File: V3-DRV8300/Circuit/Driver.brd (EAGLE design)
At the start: 61 x 56 mm, 37 parts, among them IC1 DRV8303DCA

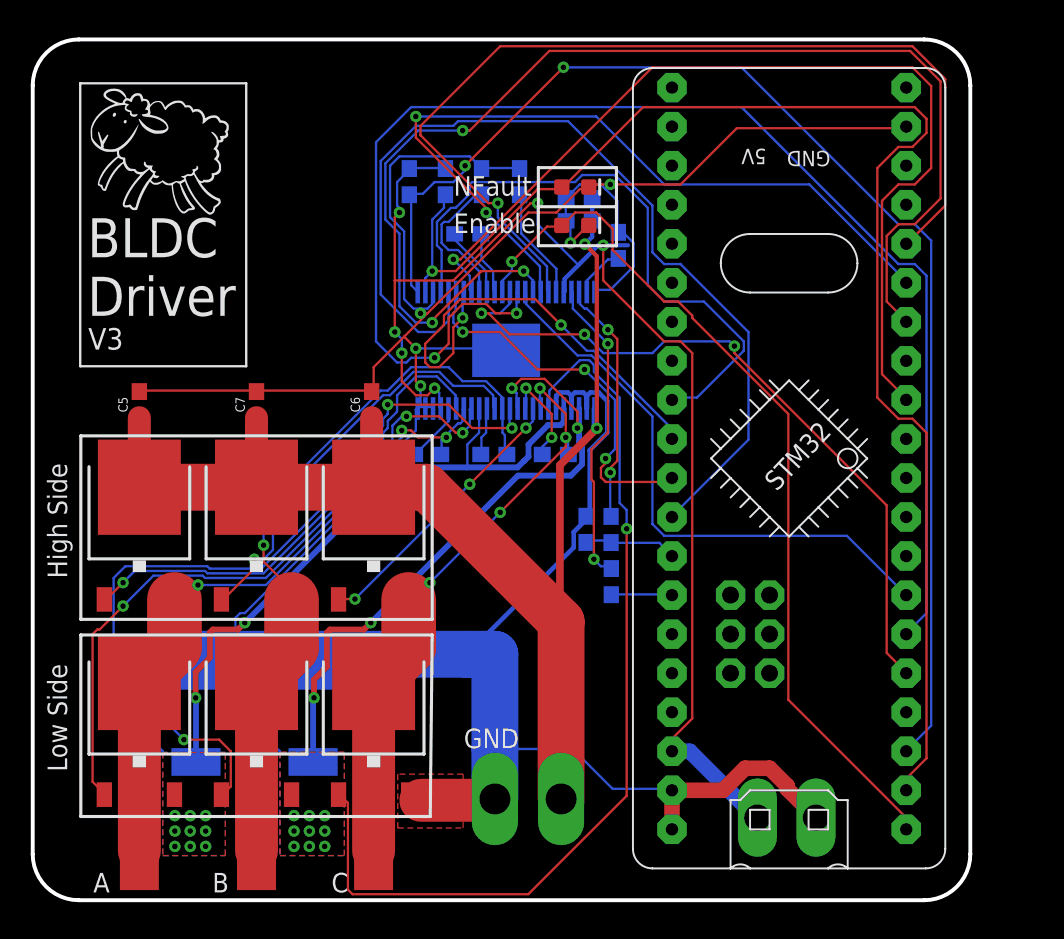
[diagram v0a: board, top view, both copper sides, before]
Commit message: Prepared for V3-DRV8300 PCB routing
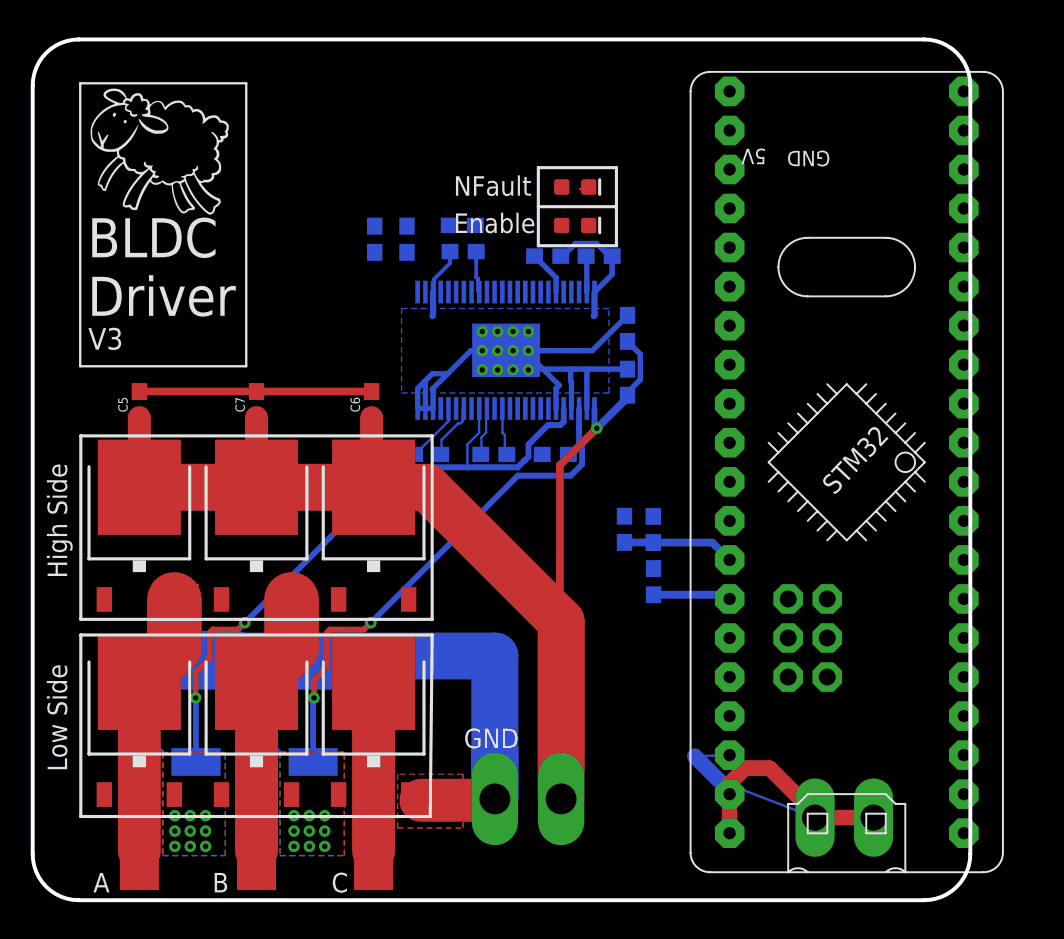
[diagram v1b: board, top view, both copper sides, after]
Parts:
- removed C10, C11: 1.0uF, SparkFun-Capacitors:0603
- added AVDD_CAP, DVDD_CAP: 1.0uF, SparkFun-Capacitors:0603
- moved C15 12.4 mm to (37.7, 32.7), turned to 90 degrees
- moved C14 7.68 mm to (37.7, 36.2), turned to 90 degrees
- moved C8 4.71 mm to (27.0, 41.2), turned to 0 degrees
- moved R6 4.51 mm to (23.4, 42.0)
- moved R4 4.37 mm to (21.2, 42.0)
- moved U$1 3.76 mm to (49.4, 33.8)
- moved 5V 3.75 mm to (51.8, 4.37)
- moved R5 2.75 mm to (39.4, 19.7)
- moved R7 2.75 mm to (39.4, 23.1)
- moved C16 2.50 mm to (37.5, 23.1)
- moved C9 0.65 mm to (26.9, 42.9), turned to 180 degrees
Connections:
- net GND: now also AVDD_CAP.2, DVDD_CAP.1; no longer C10.1, C11.2
- net N$43: now also DVDD_CAP.2; no longer C10.2
- net N$47: now also AVDD_CAP.1; no longer C11.1
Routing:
- net GND: track 232.6 -> 137.4 mm, vias 5 -> 12
- net PA9: track 92.1 -> 0.00 mm, vias 2 -> 0
- net PB13: track 91.8 -> 0.00 mm, vias 1 -> 0
- net PB14: track 82.7 -> 0.00 mm, vias 2 -> 0
- net PB6: track 79.5 -> 0.00 mm, vias 3 -> 0
- net VCC: track 87.3 -> 11.3 mm, vias 6 -> 0
- net PB8: track 63.6 -> 0.00 mm, vias 1 -> 0
- net PA7: track 62.8 -> 0.00 mm
- net PB4: track 62.4 -> 0.00 mm, vias 1 -> 0
- net GL_C: track 61.3 -> 0.00 mm, vias 1 -> 0
- net PB12: track 58.1 -> 0.00 mm, vias 1 -> 0
- net GL_B: track 54.3 -> 0.00 mm, vias 3 -> 0
- net PB7: track 51.2 -> 0.00 mm, vias 2 -> 0
- net PA8: track 46.7 -> 0.00 mm, vias 3 -> 0
- net GL_A: track 44.1 -> 0.00 mm, vias 3 -> 0
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- added copper zone on layer 16, net GND

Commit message: Prepared for V3-DRV8300 PCB routing 3
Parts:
- moved C9 1.75 mm to (26.9, 44.6)
- moved AVDD_CAP 1.25 mm to (35.9, 42.1)
- moved DVDD_CAP 1.25 mm to (32.5, 42.1)
- moved R4 1.25 mm to (21.2, 43.2)
- moved R6 1.25 mm to (23.4, 43.2)
- moved C14 1.00 mm to (38.7, 36.2)
- moved C15 1.00 mm to (38.7, 32.7)
- moved C8 1.00 mm to (27.0, 42.2)
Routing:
- net N$47: track 3.11 -> 4.36 mm
- net N$43: track 2.94 -> 4.19 mm
- net N$32: track 2.86 -> 3.86 mm
- net VIN: track 91.3 -> 92.2 mm
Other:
- board size 61 x 56 mm -> 65 x 56.8 mm

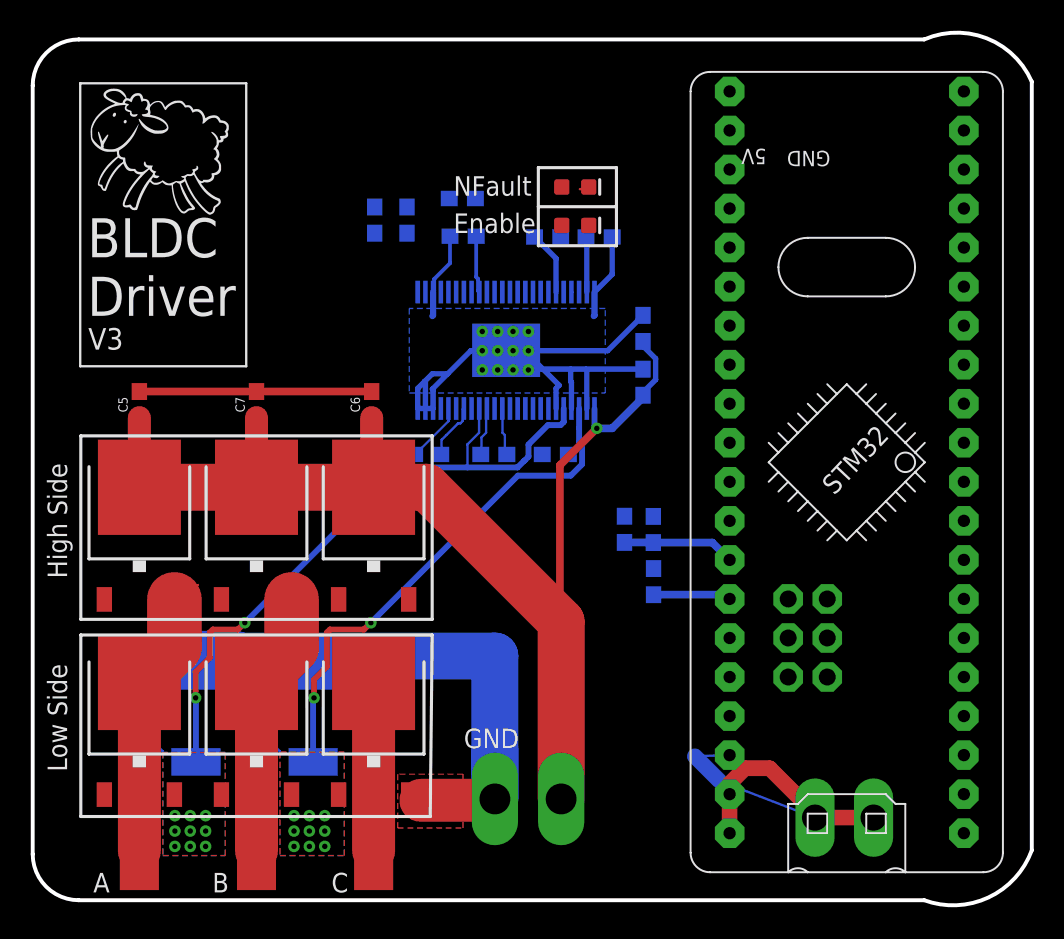
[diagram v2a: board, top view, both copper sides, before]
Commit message: V3-DRV8303 PCB Routed
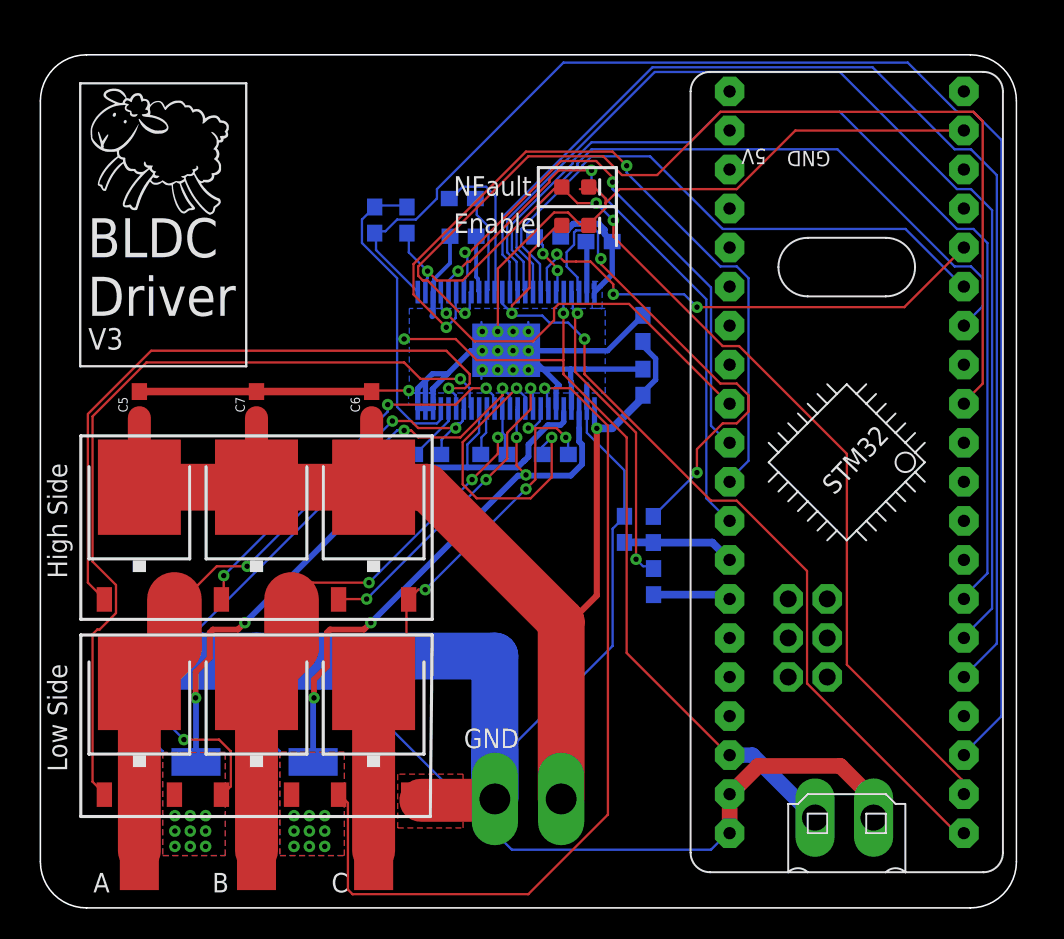
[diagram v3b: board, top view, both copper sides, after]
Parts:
- moved AVDD_CAP 0.30 mm to (35.9, 41.9)
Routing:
- net GND: track 137.6 -> 249.8 mm, vias 12 -> 13
- net PB14: track 0.00 -> 93.9 mm
- net PA8: track 0.00 -> 77.7 mm
- net PA9: track 0.00 -> 72.8 mm
- net PB13: track 0.00 -> 67.8 mm, vias 0 -> 3
- net PB4: track 0.00 -> 67.3 mm, vias 0 -> 1
- net PA10: track 0.00 -> 66.1 mm
- net VCC: track 11.3 -> 74.1 mm, vias 0 -> 2
- net PB12: track 0.00 -> 57.9 mm, vias 0 -> 2
- net GL_C: track 0.00 -> 57.5 mm, vias 0 -> 1
- net GL_A: track 0.00 -> 54.3 mm, vias 0 -> 1
- net PA6: track 0.00 -> 49.8 mm, vias 0 -> 2
- net GL_B: track 0.00 -> 48.5 mm, vias 0 -> 3
- net PB6: track 0.00 -> 44.3 mm
- net GH_A: track 0.00 -> 43.3 mm, vias 0 -> 1
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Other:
- board size 65 x 56.8 mm -> 63.5 x 55.5 mm

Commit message: Removed the signal than blocks the AGND to the powerpad; Ready for autorouting
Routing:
- net PB12: track 57.9 -> 0.00 mm, vias 2 -> 0
- net GND: track 249.8 -> 259.7 mm
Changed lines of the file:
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@@
 <drawing>
 <settings>
-<setting alwaysvectorfont="yes"/>
+<setting alwaysvectorfont="no"/>
 <setting verticaltext="up"/>
 </settings>
@@
 <via x="30.25" y="33.5" extent="1-16" drill="0.35"/>
 <via x="31.25" y="33.5" extent="1-16" drill="0.35"/>
-<wire x1="25.1226" y1="39.4174" x2="25.1226" y2="38.6376" width="0.25" layer="16"/>
-<wire x1="25.1226" y1="38.6376" x2="25.05" y2="38.565" width="0.25" layer="16"/>
-<wire x1="26.15" y1="42.2" x2="26.15" y2="40.4448" width="0.25" layer="16"/>
-<wire x1="26.15" y1="40.4448" x2="25.1226" y2="39.4174" width="0.25" layer="16"/>
+<wire x1="26.15" y1="42.2" x2="26.15" y2="40.5" width="0.25" layer="16"/>
+<wire x1="26.15" y1="40.5" x2="26.15" y2="40.4448" width="0.25" layer="16"/>
 <wire x1="29.07" y1="5.588" x2="29.07" y2="9.2964" width="3.048" layer="16"/>
 <wire x1="29.07" y1="9.2964" x2="29.07" y2="14.885621875" width="3.048" layer="16"/>
 <wire x1="29.07" y1="14.885621875" x2="13.5636" y2="14.885621875" width="3.048" layer="16"/>
 <wire x1="13.5636" y1="14.885621875" x2="7.925421875" y2="14.885621875" width="3.048" layer="16"/>
-<wire x1="38.7" y1="33.55" x2="35" y2="33.55" width="0.35" layer="16"/>
-<wire x1="35" y1="33.55" x2="34" y2="33.55" width="0.35" layer="16"/>
+<wire x1="38.7" y1="33.55" x2="34" y2="33.55" width="0.35" layer="16"/>
 <wire x1="34" y1="33.55" x2="31.45" y2="33.55" width="0.35" layer="16"/>
 <wire x1="31.45" y1="33.55" x2="30.625" y2="34.375" width="0.35" layer="16"/>
@@
 <vertex x="36.25" y="37.5"/>
 </polygon>
-<wire x1="25.05" y1="37.05" x2="25" y2="37" width="0.4" layer="16"/>
 <wire x1="33.05" y1="30.989" x2="33.05" y2="32.3" width="0.35" layer="16"/>
 <wire x1="33.05" y1="32.3" x2="33.25" y2="32.5" width="0.35" layer="16"/>
@@
 <wire x1="25" y1="32.25" x2="26" y2="33.25" width="0.35" layer="16"/>
 <wire x1="26" y1="33.25" x2="27.5" y2="34.75" width="0.35" layer="16"/>
-<wire x1="27.5" y1="34.75" x2="29.25" y2="34.75" width="0.35" layer="16"/>
+<wire x1="27.5" y1="34.75" x2="28.5" y2="34.75" width="0.35" layer="16"/>
+<wire x1="28.5" y1="34.75" x2="29.25" y2="34.75" width="0.35" layer="16"/>
 <wire x1="25.05" y1="30.989" x2="24.55" y2="30.989" width="0.35" layer="16"/>
 <wire x1="24.55" y1="30.989" x2="24.05" y2="30.989" width="0.35" layer="16"/>
@@
 <wire x1="31.3944" y1="33.528" x2="29.8" y2="34.777" width="0.1524" layer="16"/>
 <wire x1="31.3944" y1="33.528" x2="31.25" y2="33.5" width="0.1524" layer="16"/>
-<wire x1="28.194" y1="36.616996875" x2="28.194" y2="36.1188" width="0.1524" layer="16"/>
 <wire x1="28.194" y1="36.1188" x2="28.25" y2="36" width="0.1524" layer="16"/>
 <wire x1="29.718" y1="33.528" x2="29.2608" y2="33.528" width="0.1524" layer="16"/>
@@
 <wire x1="29.2608" y1="36.616996875" x2="29.2608" y2="36.1188" width="0.1524" layer="16"/>
 <wire x1="29.2608" y1="36.1188" x2="29.25" y2="36" width="0.1524" layer="16"/>
-<wire x1="31.242" y1="36.616996875" x2="31.242" y2="36.1188" width="0.1524" layer="16"/>
-<wire x1="31.242" y1="36.1188" x2="31.25" y2="36" width="0.1524" layer="16"/>
+<wire x1="31.242" y1="36.1188" x2="31.248871875" y2="36.016759375" width="0.1524" layer="16"/>
+<wire x1="31.248871875" y1="36.016759375" x2="31.25" y2="36" width="0.1524" layer="16"/>
 <wire x1="37.4904" y1="26.9748" x2="37.4904" y2="24.0792" width="0.1524" layer="16"/>
 <wire x1="35.052" y1="29.4132" x2="37.4904" y2="26.9748" width="0.1524" layer="16"/>
@@
 <via x="23.4696" y="32.1564" extent="1-16" drill="0.35"/>
 <wire x1="35.05" y1="30.989" x2="35.05" y2="32.55" width="0.35" layer="16"/>
-<wire x1="25.05" y1="38.565" x2="25.05" y2="37.05" width="0.35" layer="16"/>
 <wire x1="34.177775" y1="43.0072" x2="35.822225" y2="43.0072" width="0.4" layer="16"/>
 <wire x1="36.2072" y1="42.622225" x2="35.822225" y2="43.0072" width="0.4" layer="16"/>
@@
 <vertex x="25.2" y="32"/>
 </polygon>
+<wire x1="35.55" y1="38.565" x2="35.4486" y2="38.4636" width="0.1524" layer="16"/>
+<wire x1="34.131709375" y1="36.016759375" x2="31.248871875" y2="36.016759375" width="0.1524" layer="16"/>
+<wire x1="35.4486" y1="38.4636" x2="35.4486" y2="37.33365" width="0.1524" layer="16"/>
+<wire x1="35.4486" y1="37.33365" x2="34.131709375" y2="36.016759375" width="0.1524" layer="16"/>
+<wire x1="27.6794" y1="35.5706" x2="28.5" y2="34.75" width="0.34" layer="16"/>
+<wire x1="25.6178" y1="35.5706" x2="27.6794" y2="35.5706" width="0.34" layer="16"/>
+<wire x1="25.05" y1="38.565" x2="25.05" y2="36.1384" width="0.34" layer="16"/>
+<wire x1="25.05" y1="36.1384" x2="25.6178" y2="35.5706" width="0.34" layer="16"/>
+<wire x1="26.15" y1="40.5" x2="25.3444" y2="39.6944" width="0.25" layer="16"/>
+<wire x1="25.3444" y1="39.6944" x2="25.3444" y2="39.6572375" width="0.25" layer="16"/>
+<wire x1="25.3444" y1="39.6572375" x2="25.05" y2="39.3628375" width="0.25" layer="16"/>
+<wire x1="25.05" y1="39.3628375" x2="25.05" y2="38.565" width="0.25" layer="16"/>
+<wire x1="30.25" y1="36" x2="31.25" y2="36" width="0" layer="19" extent="1-1"/>
+<wire x1="29.25" y1="36" x2="30.25" y2="36" width="0" layer="19" extent="1-1"/>
+<wire x1="28.25" y1="36" x2="29.25" y2="36" width="0" layer="19" extent="1-1"/>
+<wire x1="31.25" y1="34.75" x2="31.25" y2="36" width="0" layer="19" extent="1-1"/>
+<wire x1="30.25" y1="34.75" x2="31.25" y2="34.75" width="0" layer="19" extent="1-1"/>
+<wire x1="29.8" y1="34.777" x2="30.25" y2="34.75" width="0" layer="19" extent="16-16"/>
+<wire x1="29.25" y1="34.75" x2="29.8" y2="34.777" width="0" layer="19" extent="16-16"/>
+<wire x1="28.25" y1="34.75" x2="29.25" y2="34.75" width="0" layer="19" extent="1-1"/>
+<wire x1="30.25" y1="33.5" x2="29.25" y2="33.5" width="0" layer="19" extent="1-1"/>
+<wire x1="28.25" y1="33.5" x2="29.25" y2="33.5" width="0" layer="19" extent="1-1"/>
+<wire x1="35.05" y1="30.989" x2="34.05" y2="30.989" width="0" layer="19" extent="16-16"/>
+<wire x1="23.46" y1="5.868" x2="24.25" y2="5.5" width="0" layer="19" extent="1-1"/>
+<wire x1="23.5" y1="32.1564" x2="24.05" y2="30.989" width="0" layer="19" extent="16-16"/>
 </signal>
 <signal name="N$4">
@@
 <contactref element="IC1" pad="12"/>
 <contactref element="D2" pad="A"/>
-<wire x1="30.1752" y1="37.6856" x2="30.1752" y2="37.1856" width="0.1524" layer="1"/>
-<wire x1="29.5656" y1="37.7952" x2="30.1752" y2="37.1856" width="0.1524" layer="16"/>
-<wire x1="29.5656" y1="38.5572" x2="29.5656" y2="37.7952" width="0.1524" layer="16"/>
-<wire x1="29.5656" y1="38.5572" x2="29.55" y2="38.565" width="0.1524" layer="16"/>
-<wire x1="58.9788" y1="3.5052" x2="59.436" y2="3.5052" width="0.1524" layer="1"/>
-<wire x1="49.3776" y1="13.1064" x2="58.9788" y2="3.5052" width="0.1524" layer="1"/>
-<wire x1="49.3776" y1="20.4216" x2="49.3776" y2="13.1064" width="0.1524" layer="1"/>
-<wire x1="44.8056" y1="24.9936" x2="49.3776" y2="20.4216" width="0.1524" layer="1"/>
-<wire x1="43.1292" y1="24.9936" x2="44.8056" y2="24.9936" width="0.1524" layer="1"/>
-<wire x1="34.8996" y1="33.2232" x2="43.1292" y2="24.9936" width="0.1524" layer="1"/>
-<wire x1="34.8996" y1="35.5092" x2="34.8996" y2="33.2232" width="0.1524" layer="1"/>
-<wire x1="33.8328" y1="36.576" x2="34.8996" y2="35.5092" width="0.1524" layer="16"/>
-<wire x1="32.6136" y1="36.576" x2="33.8328" y2="36.576" width="0.1524" layer="16"/>
-<wire x1="32.1564" y1="37.0332" x2="32.6136" y2="36.576" width="0.1524" layer="16"/>
-<wire x1="30.3276" y1="37.0332" x2="32.1564" y2="37.0332" width="0.1524" layer="16"/>
-<wire x1="30.1752" y1="37.1856" x2="30.3276" y2="37.0332" width="0.1524" layer="16"/>
-<wire x1="59.436" y1="3.5052" x2="59.581" y2="3.36" width="0.1524" layer="1"/>
-<via x="30.1752" y="37.1856" extent="1-16" drill="0.35"/>
-<via x="34.8996" y="35.5092" extent="1-16" drill="0.35"/>
-<wire x1="33.423" y1="42.9" x2="33.123" y2="42.9" width="0.1524" layer="1"/>
-<wire x1="33.123" y1="42.9" x2="31.323" y2="41.1" width="0.1524" layer="1"/>
-<wire x1="31.323" y1="41.1" x2="31.323" y2="38.8334" width="0.1524" layer="1"/>
-<wire x1="31.323" y1="38.8334" x2="30.1752" y2="37.6856" width="0.1524" layer="1"/>
+<wire x1="29.55" y1="38.565" x2="33.423" y2="42.9" width="0" layer="19" extent="1-16"/>
+<wire x1="59.581" y1="3.36" x2="29.55" y2="38.565" width="0" layer="19" extent="16-16"/>
 </signal>
 <signal name="PB13">
